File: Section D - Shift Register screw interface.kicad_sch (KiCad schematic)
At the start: 1 part

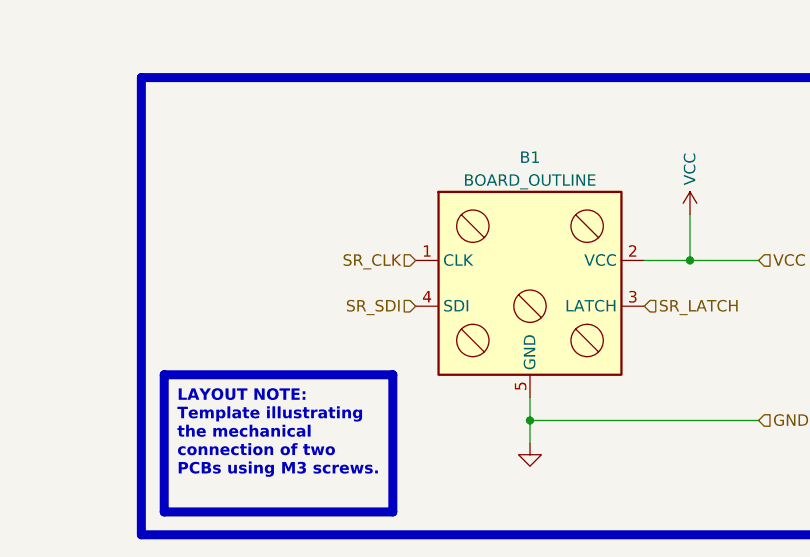
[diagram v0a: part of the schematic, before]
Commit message: reassign SR signals for clean design (fixes #4)
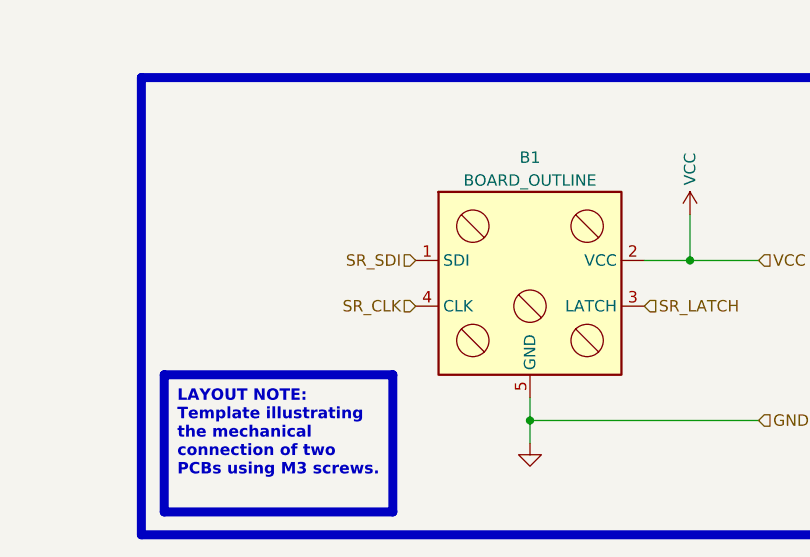
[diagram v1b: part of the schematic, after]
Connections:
- net SR_CLK: now also B1.4 (CLK); no longer B1.1 (CLK)
- net SR_SDI: now also B1.1 (SDI); no longer B1.4 (SDI)
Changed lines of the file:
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@@
 	(hierarchical_label "SR_SDI"
 		(shape input)
-		(at 132.08 88.9 180)
+		(at 132.08 83.82 180)
 		(effects
 			(font
@@
 	(hierarchical_label "SR_CLK"
 		(shape input)
-		(at 132.08 83.82 180)
+		(at 132.08 88.9 180)
 		(effects
 			(font

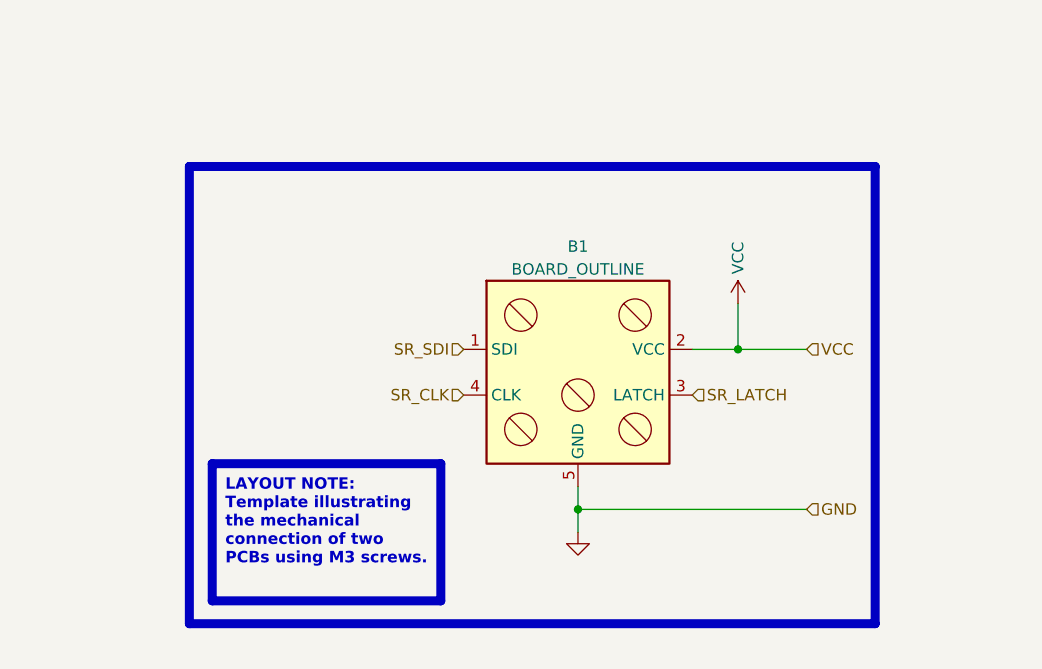
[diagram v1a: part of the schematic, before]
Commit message: documentation update / block diagram
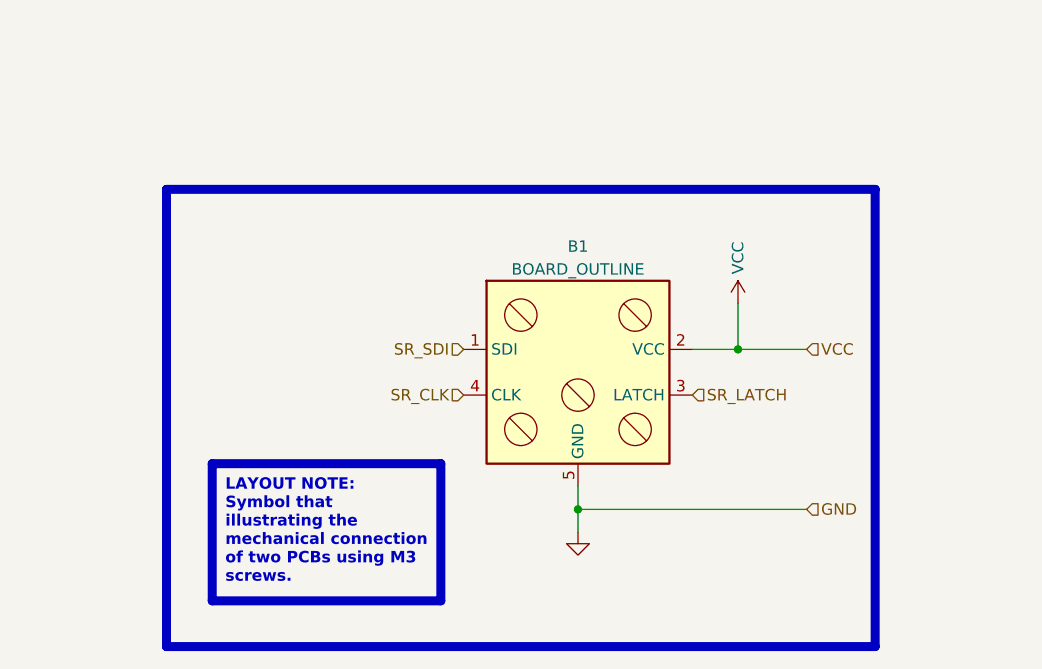
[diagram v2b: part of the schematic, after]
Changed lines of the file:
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@@
 	)
 	(rectangle
-		(start 101.6 63.5)
-		(end 177.8 114.3)
+		(start 99.06 66.04)
+		(end 177.8 116.84)
 		(stroke
 			(width 1)
@@
 		)
 	)
-	(text_box "LAYOUT NOTE:\nTemplate illustrating the mechanical connection of two PCBs using M3 screws."
+	(text_box "LAYOUT NOTE:\nSymbol that illustrating the mechanical connection of two PCBs using M3 screws."
 		(exclude_from_sim no)
 		(at 104.14 96.52 0)
